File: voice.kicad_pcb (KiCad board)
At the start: 2 copper layers, 133.3 x 50 mm, 416 parts, among them J1 DDR3-DIMM, Q1 2SA1832, Q10 2SA1832, Q11 2SA1832, Q12 2SK208-GR, Q13 2SK208-GR, Q14 2SA1832, Q15 2SA1832, Q16 2SA1618, Q17 2SA1832, Q18 2SA1832, Q19 2SK208-GR, Q2 2SA1832, Q20 2SA1832, Q21 2SC4738, Q22 2SC4738, Q23 2SC4738, Q24 2SC4207, Q25 2SA1618, Q26 2SA1618, Q27 2SC4207, Q28 2SC4738, Q29 MMBF4391LT1G, Q3 2SA1832, Q30 MMBF4391LT1G, Q31 2SC4207, Q32 2SC4207, Q33 PMBT2369, Q34 PMBT2369, Q35 2SA1832, Q36 2SA1832, Q37 PMBT2369, Q38 2SC4738, Q4 2SA1832, Q5 2SK208-GR, Q6 2SK208-GR, Q7 2SK208-GR, Q8 2SK208-GR, Q9 2SK208-GR, U1 CD4053, U10 LM13700, U11 TL072-, U12 LM13700, U13 TA75S558F, U14 LM13700, U15 RC4558, U16 TA75S558F, U17 NE555, U18 NE555, U19 TL074-, U2 LM13700, U20 CD4052, U21 CD4052, U22 TL074-, U23 TL072-, U24 TL074-, U25 TA75S558F, U26 TL072-, U27 TL074-, U3 TA75S558F, U30 CD4052, U31 CD4052, U4 CD4053, U5 LM13700, U6 TA75S558F, U7 LM13700, U8 LM13700, U9 LM13700

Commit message: first of many many days of routing
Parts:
- VR1, VR2: footprint MyModules:Bourns_3362P -> MyModules:TT-BI-67W
- moved VR1 93.5 mm to (92.0, 30.5), turned to 180 degrees
- moved R222 68.0 mm to (110.2, 48.8), turned to 90 degrees
- moved R228 67.7 mm to (107.8, 51.0)
- moved R235 65.9 mm to (108.0, 53.0), turned to 180 degrees
- moved C35 65.9 mm to (95.8, 65.5), turned to 90 degrees
- moved R211 63.0 mm to (114.8, 51.8)
- moved R181 63.0 mm to (97.0, 68.8)
- moved U25 60.5 mm to (114.8, 54.8), turned to 180 degrees
- moved U2 60.2 mm to (132.5, 47.0)
- moved R193 58.1 mm to (115.0, 57.5), turned to 180 degrees
- moved R224 56.9 mm to (112.8, 60.8), turned to 90 degrees
- moved D9 55.9 mm to (114.8, 60.5), turned to 270 degrees
- moved Q33 54.4 mm to (117.2, 60.5)
- moved R214 53.3 mm to (114.5, 64.0), turned to 270 degrees
- moved Q35 51.8 mm to (116.5, 64.2), turned to 270 degrees
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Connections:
- U27 pad 1: Net-(R232-Pad1) -> Net-(R226-Pad1)
- U27 pad 2: Net-(R235-Pad2) -> Net-(R224-Pad2)
- U27 pad 3: Net-(R242-Pad2) -> Net-(R228-Pad2)
- U27 pad 5: Net-(R228-Pad2) -> Net-(R242-Pad2)
- U27 pad 6: Net-(R224-Pad2) -> Net-(R235-Pad2)
- U27 pad 7: Net-(R226-Pad1) -> Net-(R232-Pad1)
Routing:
- net Net-(Q31-Pad2): track 9.60 -> 0.00 mm
- net Net-(R224-Pad2): track 0.00 -> 5.72 mm
- net Net-(C27-Pad1): track 0.00 -> 5.48 mm
- net Net-(C29-Pad2): track 4.42 -> 9.17 mm
- net Net-(D5-Pad2): track 0.00 -> 1.79 mm
- net Net-(Q31-Pad4): track 5.00 -> 5.58 mm

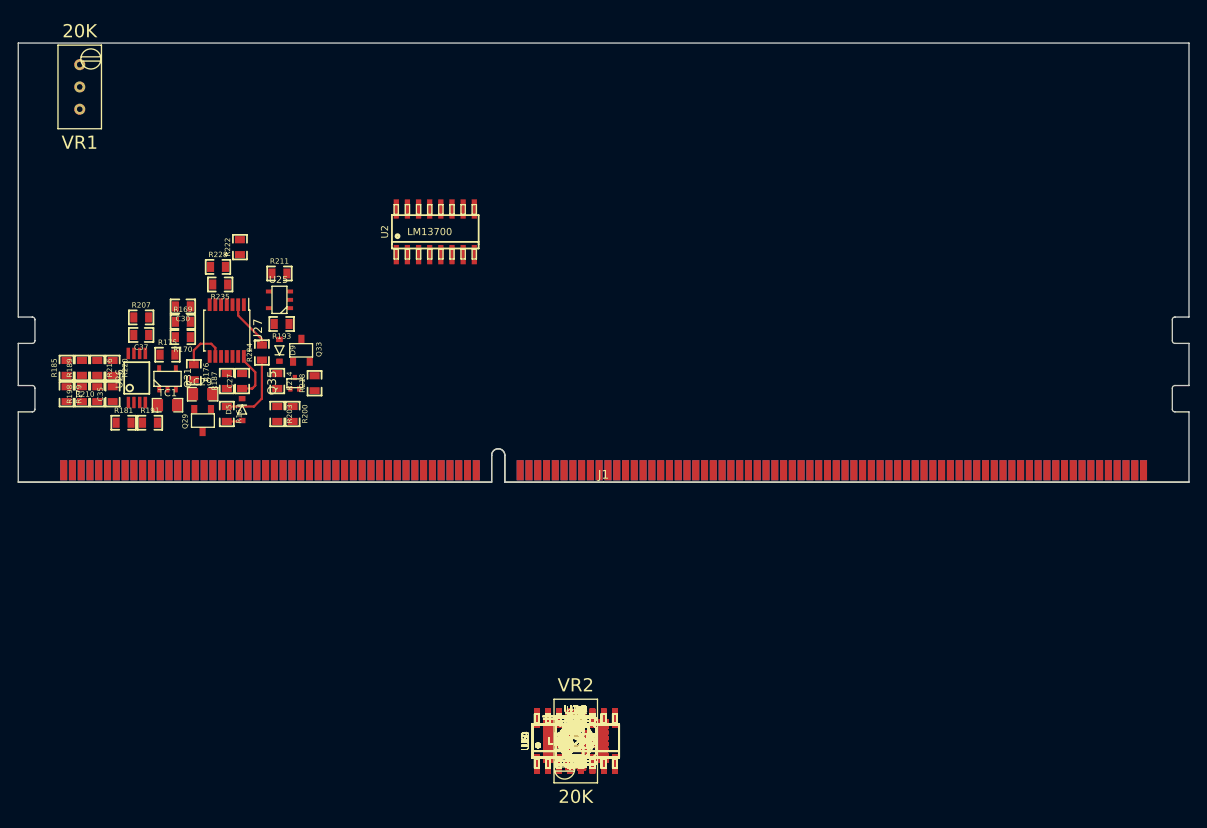
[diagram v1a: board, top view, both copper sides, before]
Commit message: VCO1 mostly placed
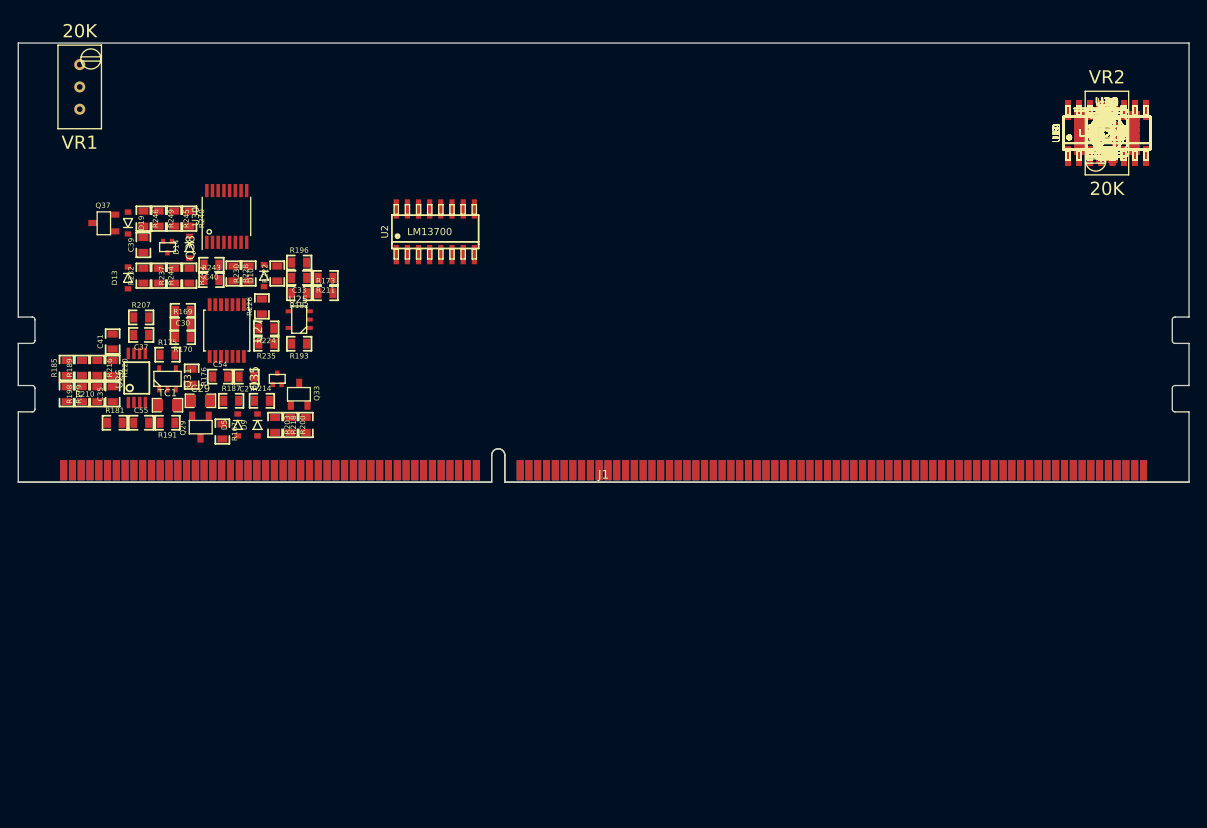
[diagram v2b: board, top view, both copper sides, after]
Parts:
- moved C1 92.0 mm to (209.0, 35.8)
- moved C10 92.0 mm to (209.0, 35.8)
- moved C11 92.0 mm to (209.0, 35.8)
- moved C12 92.0 mm to (209.0, 35.8)
- moved C13 92.0 mm to (209.0, 35.8)
- moved C14 92.0 mm to (209.0, 35.8)
- moved C15 92.0 mm to (209.0, 35.8)
- moved C16 92.0 mm to (209.0, 35.8)
- moved C17 92.0 mm to (209.0, 35.8)
- moved C18 92.0 mm to (209.0, 35.8)
- moved C19 92.0 mm to (209.0, 35.8)
- moved C2 92.0 mm to (209.0, 35.8)
- moved C20 92.0 mm to (209.0, 35.8)
- moved C21 92.0 mm to (209.0, 35.8)
- moved C22 92.0 mm to (209.0, 35.8)
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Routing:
- net Net-(C29-Pad2): track 9.17 -> 0.00 mm
- net Net-(R224-Pad2): track 5.72 -> 0.00 mm
- net Net-(Q31-Pad4): track 5.58 -> 0.00 mm
- net Net-(C27-Pad1): track 5.48 -> 0.00 mm
- net Net-(D5-Pad2): track 1.79 -> 0.00 mm

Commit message: placing
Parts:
- removed VR1, VR2: 20K, MyModules:TT-BI-67W
- added R250: 10K, MyModules:SM0603-R-JRL, F.Cu at (94.0, 65.5)
- added R251: 10K, MyModules:SM0603-R-JRL, F.Cu at (151.7, 85.6)
- added TP10: TEST_POINT, MyModules:TEST_POINT_SMALL, F.Cu at (94.2, 70.0)
- added TP11, TP13: TEST_POINT, MyModules:TEST_POINT_SMALL, F.Cu at (151.7, 85.6)
- added TP12: TEST_POINT, MyModules:TEST_POINT_SMALL, F.Cu at (92.2, 61.8)
- moved D18 121.5 mm to (89.8, 59.0)
- moved R248 116.9 mm to (94.0, 56.5), turned to 270 degrees
- moved D16 114.4 mm to (96.0, 53.5), turned to 90 degrees
- moved R241 109.9 mm to (100.8, 54.5), turned to 180 degrees
- moved U1 100.3 mm to (108.8, 34.8), turned to 90 degrees
- moved R247 96.7 mm to (112.8, 44.8), turned to 270 degrees
- moved D17 93.7 mm to (115.8, 44.8), turned to 270 degrees
- moved U4 92.0 mm to (117.0, 34.8), turned to 90 degrees
- moved U5 82.5 mm to (126.5, 34.8)
- moved U2 35.6 mm to (99.0, 35.0)
- moved R220 3.47 mm to (94.0, 59.5)
- moved C41 3.00 mm to (95.8, 62.5), turned to 270 degrees
- moved D13 2.50 mm to (97.5, 49.8), turned to 270 degrees
- moved R179 1.75 mm to (88.8, 65.5)
- moved R185 1.75 mm to (88.8, 62.5), turned to 270 degrees
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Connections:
- U30 pad 1: VCO1_TRI -> VCO1_SQUARE
- U30 pad 4: VCO1_SQUARE -> VCO1_SAW
- U30 pad 5: VCO1_SAW -> VCO1_TRI
- U30 pad 7: GND -> -5V
- U30 pad 8: -5V -> GND
- U31 pad 7: GND -> -5V
- U31 pad 8: -5V -> GND
- U4 pad 7: GND -> -5V
- U4 pad 8: -5V -> GND
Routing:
- net Net-(Q31-Pad2): track 0.00 -> 10.5 mm
- net +10V: track 0.00 -> 6.37 mm
- net Net-(R232-Pad1): track 0.00 -> 5.74 mm
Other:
- net class Default: clearance 0.2032 -> 0.2; trace_width 0.254 -> 0.25; via_dia 1.016 -> 0.8; via_drill 0.508 -> 0.4
- net class POWER: clearance 0.2032 -> 0.2; trace_width 0.3048 -> 0.35; via_dia 1.016 -> 1; via_drill 0.508 -> 0.5
- rule trace_clearance: 0.2032 -> 0.2

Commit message: placing...
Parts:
- moved R16 118.8 mm to (90.2, 33.2), turned to 90 degrees
- moved R17 116.4 mm to (92.8, 41.5), turned to 90 degrees
- moved Q1 116.3 mm to (92.8, 32.0), turned to 180 degrees
- moved Q2 116.3 mm to (92.8, 37.8), turned to 180 degrees
- moved R3 115.2 mm to (94.0, 28.8), turned to 180 degrees
- moved R5 114.6 mm to (94.5, 41.5), turned to 270 degrees
- moved R13 112.9 mm to (96.2, 41.5), turned to 90 degrees
- moved R8 112.3 mm to (97.0, 27.2)
- moved R11 112.2 mm to (97.0, 28.8)
- moved R6 109.9 mm to (99.2, 41.5), turned to 270 degrees
- moved R4 109.1 mm to (100.2, 27.2)
- moved R12 109.0 mm to (100.2, 28.8), turned to 180 degrees
- moved R14 108.2 mm to (101.0, 41.5), turned to 90 degrees
- moved U3 102.8 mm to (106.2, 32.2)
- moved R15 102.8 mm to (106.2, 38.0), turned to 180 degrees
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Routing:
- net +12V: track 0.00 -> 1.54 mm, vias 0 -> 1
- net Net-(R12-Pad2): track 0.00 -> 1.50 mm
- net Net-(R11-Pad2): track 0.00 -> 1.50 mm

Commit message: placing more
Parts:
- moved U6 93.2 mm to (115.9, 34.8), turned to 270 degrees
- moved R26 89.4 mm to (119.9, 28.8)
- moved R23 86.4 mm to (122.9, 28.8)
- moved R217 86.3 mm to (127.0, 62.5), turned to 270 degrees
- moved C42 84.6 mm to (128.8, 62.5), turned to 270 degrees
- moved C56 83.4 mm to (132.2, 68.5)
- moved R19 83.4 mm to (125.9, 28.8), turned to 180 degrees
- moved U23 82.3 mm to (131.5, 63.5)
- moved R28 80.5 mm to (128.9, 28.8)
- moved TC2 80.1 mm to (135.0, 66.5)
- moved Q3 80.0 mm to (129.1, 31.0)
- moved R21 79.4 mm to (129.6, 33.0), turned to 180 degrees
- moved R29 79.4 mm to (129.6, 34.8)
- moved R32 79.4 mm to (129.6, 36.2)
- moved Q32 79.1 mm to (135.0, 63.8), turned to 90 degrees
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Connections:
- U7 pad 12: Net-(C8-Pad1) -> Net-(R44-Pad2)
- U7 pad 13: Net-(R45-Pad1) -> Net-(R48-Pad1)
- U7 pad 14: GND -> Net-(R33-Pad1)
- U7 pad 16: Net-(R38-Pad1) -> Net-(Q4-Pad3)
- U8 pad 12: Net-(C10-Pad1) -> Net-(C8-Pad1)
- U8 pad 13: Net-(R47-Pad1) -> Net-(R45-Pad1)
- U8 pad 16: Net-(R40-Pad1) -> Net-(R38-Pad1)
- U9 pad 12: Net-(R44-Pad2) -> Net-(C10-Pad1)
- U9 pad 13: Net-(R48-Pad1) -> Net-(R47-Pad1)
- U9 pad 14: Net-(R33-Pad1) -> GND
- U9 pad 16: Net-(Q4-Pad3) -> Net-(R40-Pad1)
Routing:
- net +12V: track 1.54 -> 0.00 mm, vias 1 -> 0
- net Net-(R12-Pad2): track 1.50 -> 0.00 mm
- net Net-(R11-Pad2): track 1.50 -> 0.00 mm

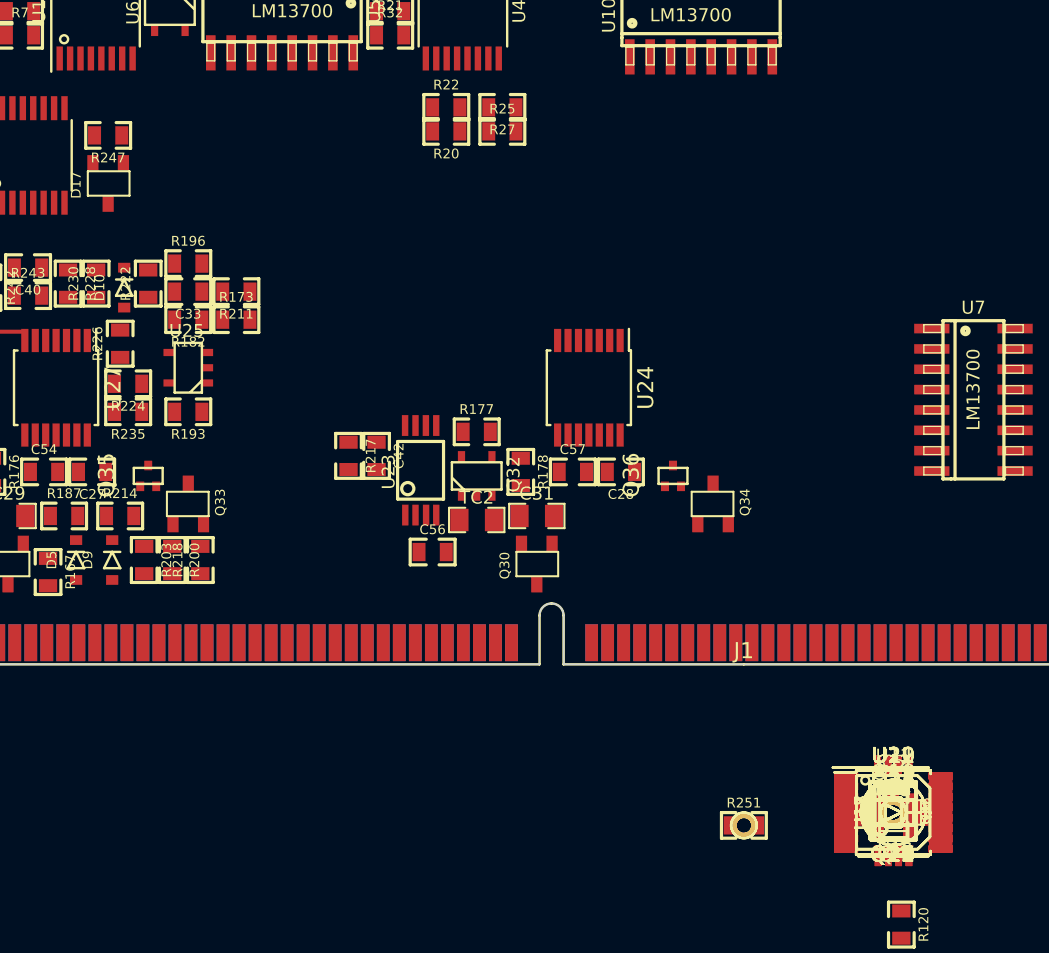
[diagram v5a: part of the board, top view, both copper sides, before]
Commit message: more VCO2 placement
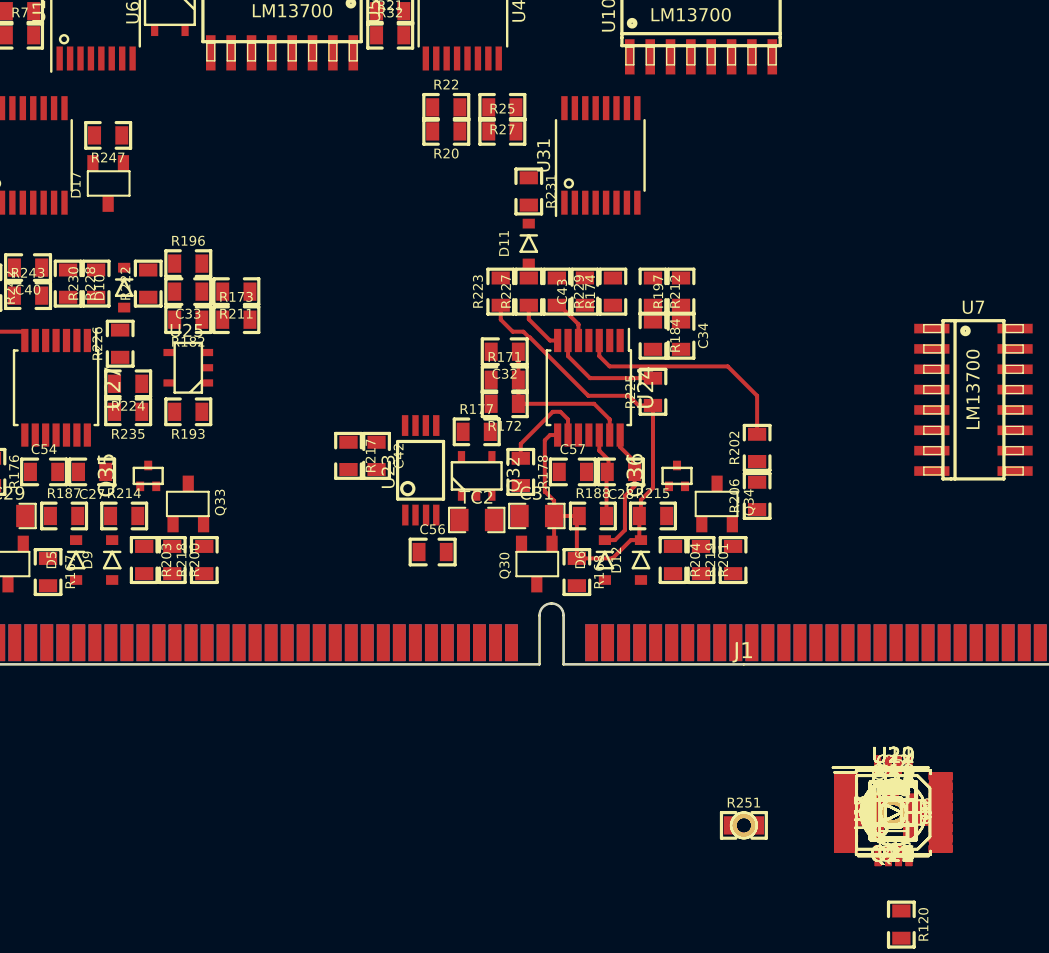
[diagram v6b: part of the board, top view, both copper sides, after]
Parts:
- moved R231 44.9 mm to (138.2, 46.0), turned to 270 degrees
- moved U31 44.9 mm to (142.8, 43.8), turned to 90 degrees
- moved D11 42.2 mm to (138.2, 49.2), turned to 90 degrees
- moved R223 40.7 mm to (136.5, 52.2), turned to 90 degrees
- moved R227 39.7 mm to (138.2, 52.2), turned to 90 degrees
- moved R229 38.7 mm to (140.0, 52.2), turned to 270 degrees
- moved C43 37.8 mm to (141.8, 52.2), turned to 90 degrees
- moved C32 37.6 mm to (136.8, 56.0), turned to 180 degrees
- moved R174 36.9 mm to (143.5, 52.2), turned to 90 degrees
- moved R171 36.3 mm to (136.8, 57.8)
- moved R212 35.8 mm to (146.0, 52.2), turned to 270 degrees
- moved R172 35.2 mm to (136.8, 59.2), turned to 180 degrees
- moved R197 35.1 mm to (147.8, 52.2), turned to 90 degrees
- moved R184 33.3 mm to (146.0, 55.0), turned to 270 degrees
- moved C34 32.6 mm to (147.8, 55.0), turned to 270 degrees
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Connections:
- U24 pad 1: Net-(C31-Pad2) -> Net-(C34-Pad2)
- U24 pad 10: Net-(D7-Pad1) -> GND
- U24 pad 12: Net-(R229-Pad2) -> Net-(C28-Pad2)
- U24 pad 13: Net-(R225-Pad2) -> SYNC
- U24 pad 14: Net-(R227-Pad1) -> Net-(C28-Pad1)
- U24 pad 2: Net-(Q32-Pad4) -> Net-(C34-Pad1)
- U24 pad 3: GND -> Net-(D7-Pad1)
- U24 pad 5: Net-(C28-Pad2) -> Net-(R229-Pad2)
- U24 pad 6: SYNC -> Net-(R225-Pad2)
- U24 pad 7: Net-(C28-Pad1) -> Net-(R227-Pad1)
- U24 pad 8: Net-(C34-Pad2) -> Net-(C31-Pad2)
- U24 pad 9: Net-(C34-Pad1) -> Net-(Q32-Pad4)
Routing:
- net Net-(C31-Pad2): track 0.00 -> 38.4 mm
- net Net-(D7-Pad1): track 0.00 -> 14.2 mm
- net SYNC: track 0.00 -> 10.3 mm
- net Net-(C28-Pad1): track 0.00 -> 8.06 mm
- net Net-(R225-Pad2): track 0.00 -> 6.84 mm
- net Net-(Q32-Pad4): track 0.00 -> 6.01 mm
- net Net-(C28-Pad2): track 0.00 -> 5.34 mm
- net Net-(R227-Pad1): track 0.00 -> 3.22 mm
- net Net-(R229-Pad2): track 0.00 -> 2.86 mm

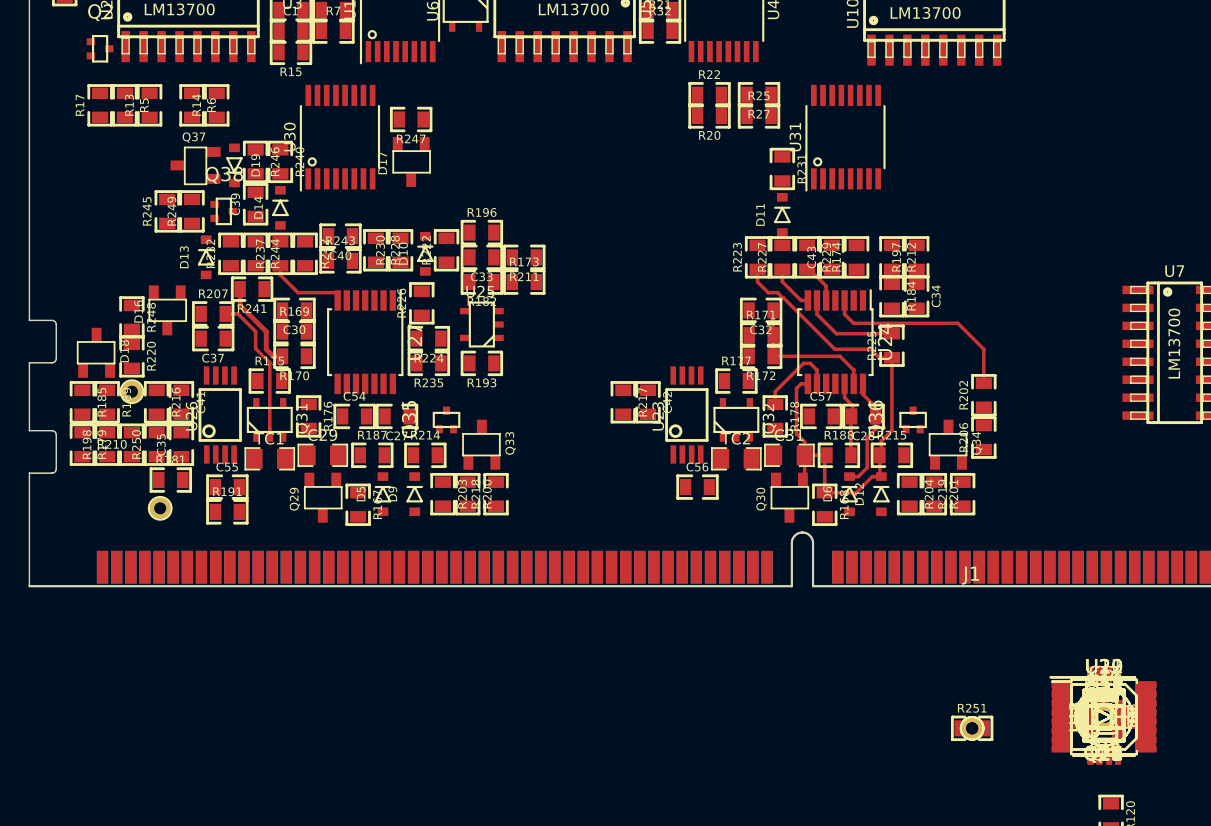
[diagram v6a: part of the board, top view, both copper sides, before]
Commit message: VCO2 basically placed
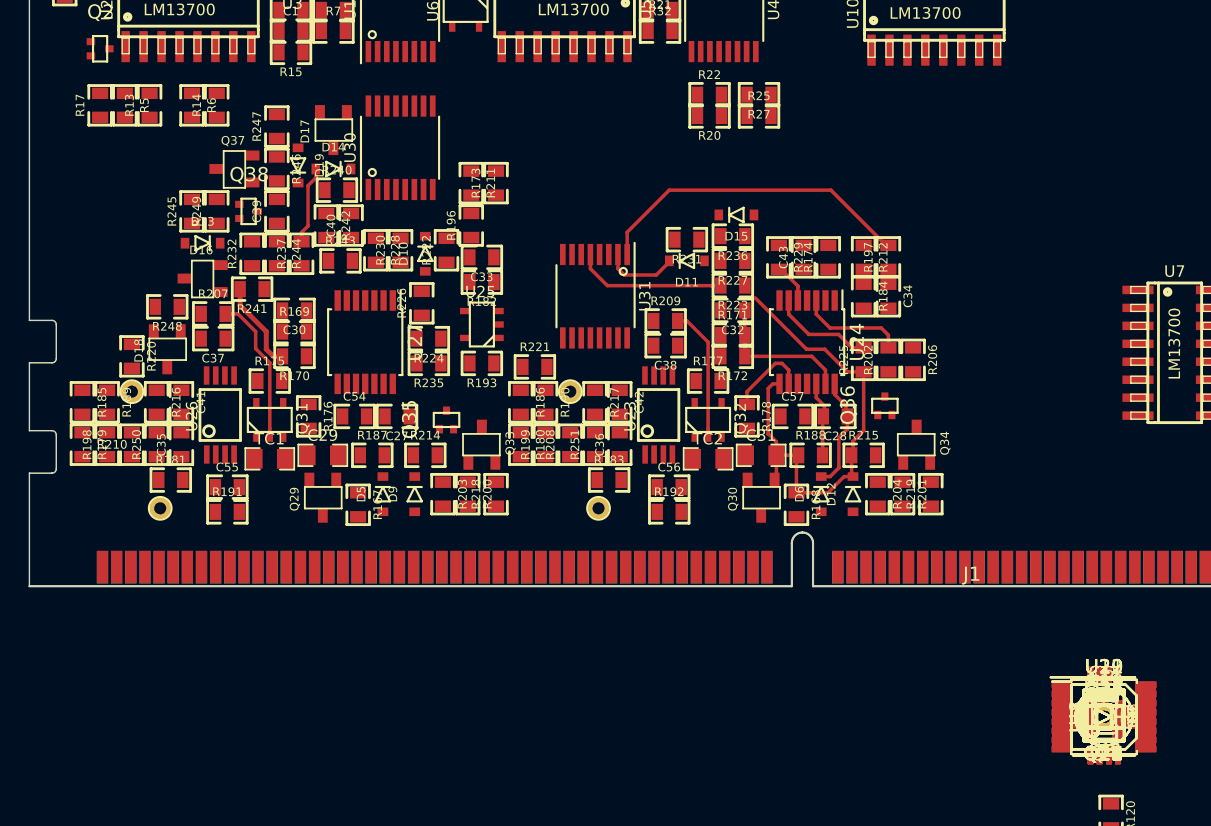
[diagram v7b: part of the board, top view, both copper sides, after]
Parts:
- moved R221 47.3 mm to (120.8, 60.0)
- moved R186 46.9 mm to (119.8, 62.5), turned to 270 degrees
- moved R180 45.5 mm to (119.8, 65.5), turned to 270 degrees
- moved R190 45.3 mm to (121.5, 62.5), turned to 270 degrees
- moved D15 44.0 mm to (135.0, 49.2), turned to 180 degrees
- moved R199 43.9 mm to (121.5, 65.5), turned to 90 degrees
- moved R236 43.0 mm to (134.8, 50.8), turned to 180 degrees
- moved R208 42.4 mm to (123.2, 65.5), turned to 90 degrees
- moved R209 41.8 mm to (130.0, 56.8)
- moved C38 40.6 mm to (130.0, 58.5), turned to 180 degrees
- moved C36 39.3 mm to (126.8, 65.5), turned to 90 degrees
- moved R183 38.8 mm to (126.0, 68.0)
- moved TP13 37.1 mm to (123.2, 61.8), turned to 180 degrees
- moved R192 34.0 mm to (130.2, 70.2)
- moved R251 33.4 mm to (125.0, 65.5), turned to 90 degrees
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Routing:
- net VCO2_SINE: track 0.00 -> 22.9 mm
- net VCO2_SAW: track 0.00 -> 10.7 mm
- net Net-(Q32-Pad2): track 0.00 -> 9.47 mm
- net Net-(D7-Pad1): track 14.2 -> 7.59 mm
- net Net-(D14-Pad2): track 0.00 -> 5.57 mm
- net VCO2_PULSE: track 0.00 -> 5.28 mm
- net Net-(R232-Pad1): track 5.74 -> 0.57 mm
- net Net-(C31-Pad2): track 38.4 -> 34.6 mm
- net Net-(R227-Pad1): track 3.22 -> 0.00 mm
